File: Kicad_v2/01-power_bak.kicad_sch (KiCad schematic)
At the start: 45 parts, among them IC2 BQ25630YBGR, J1 USB4105-GF-A-060, U11 RT6158HWSC, U2 TCR3UG33A_LF, U4 TPS61253F, U7 USBLC6-2SC6

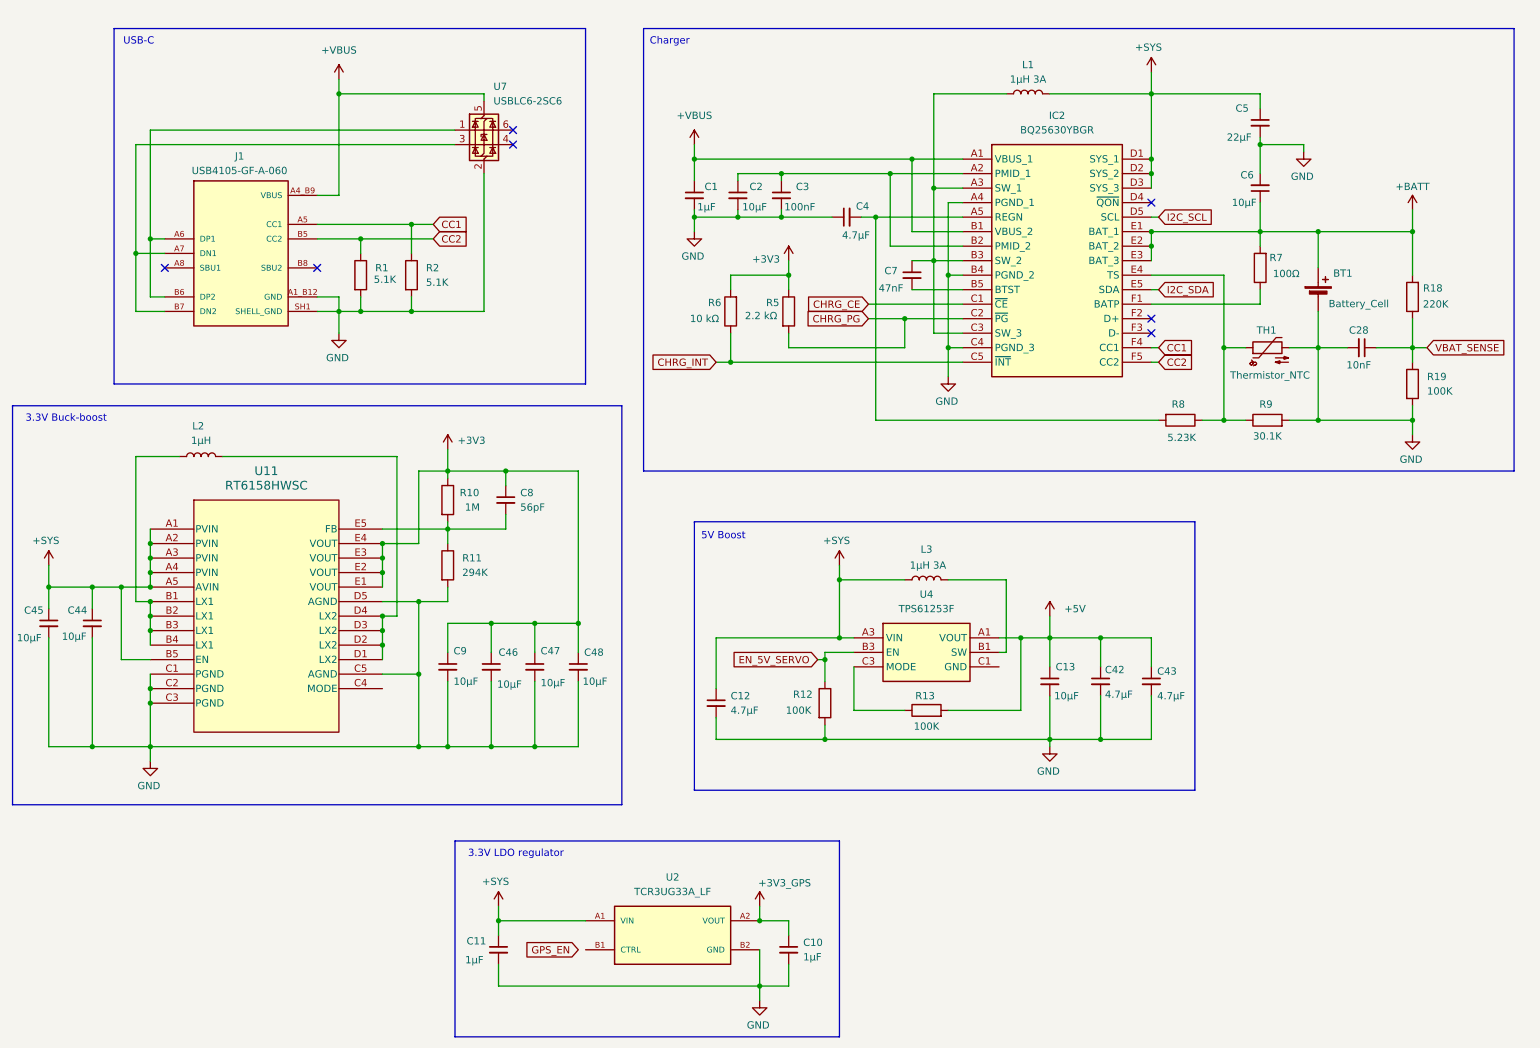
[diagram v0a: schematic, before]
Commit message: KiCad Power schema herschikt
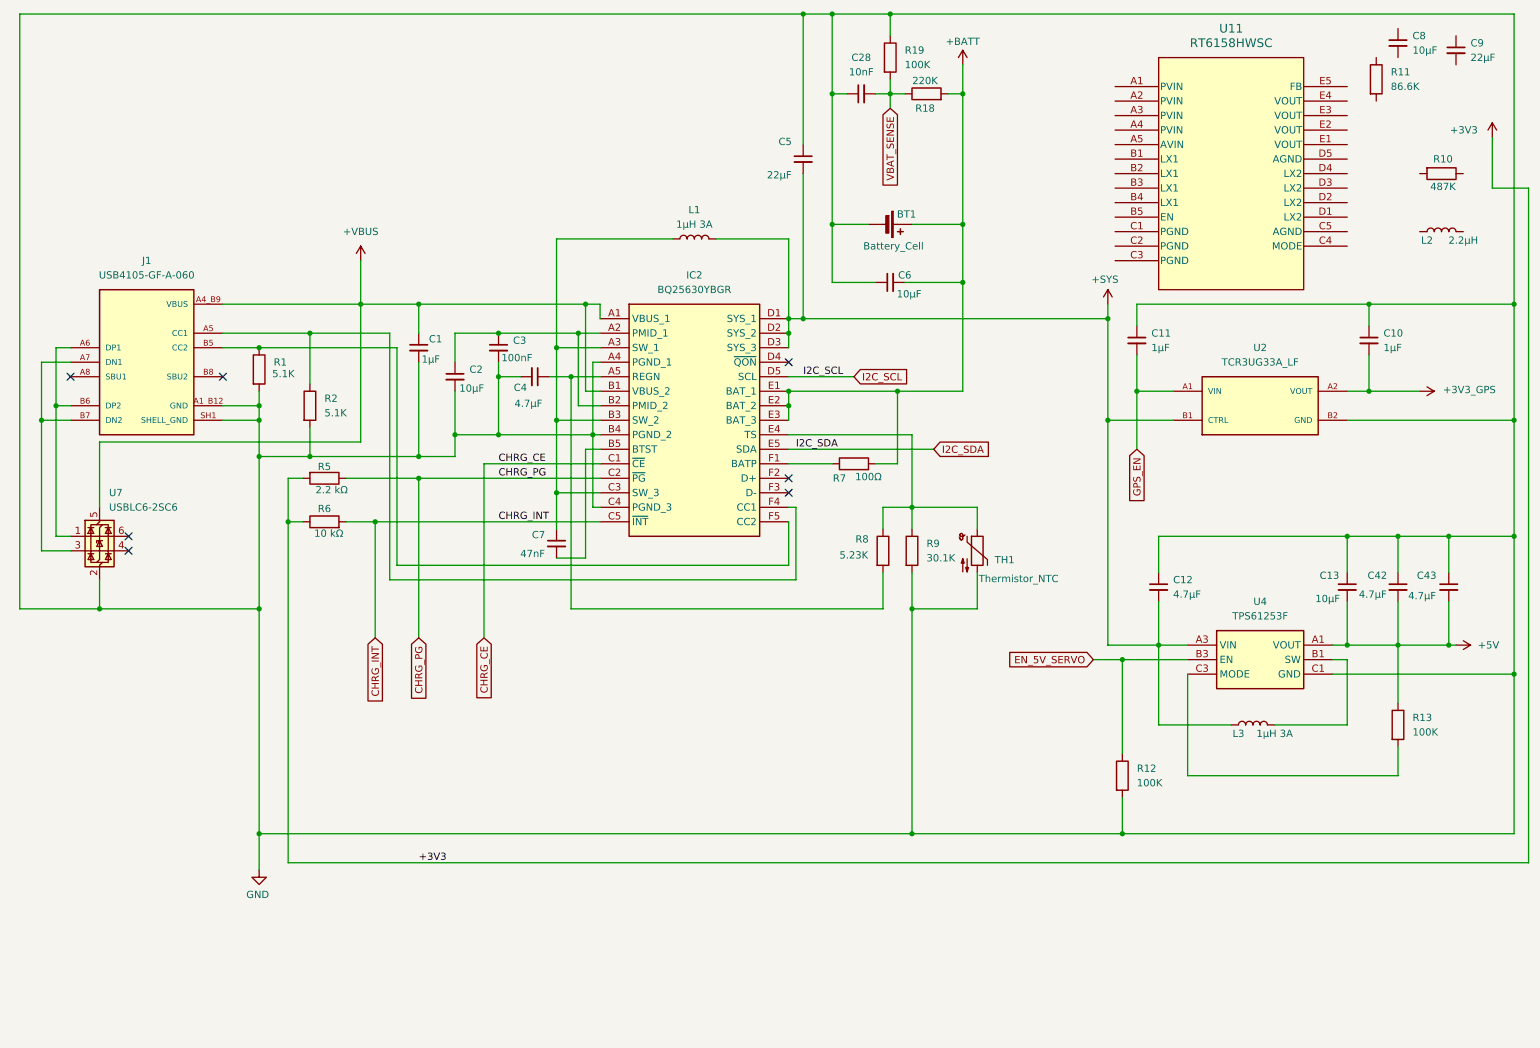
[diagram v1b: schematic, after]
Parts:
- removed C44, C45, C46, C47, C48: 10µF, Capacitor_SMD:C_0603_1608Metric_Pad1.08x0.95mm_HandSolder, symbol Device:C_Small
- C8: value 56pF -> 10µF
- C9: value 10µF -> 22µF
- L2: value 1µH -> 2.2µH
- R10: value 1M -> 487K
- R11: value 294K -> 86.6K
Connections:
- net +3V3: now also R5.2, R6.1; no longer C8.1, C9.1, R10.1, R5.1, R6.2, U11.E1 (VOUT), U11.E2 (VOUT), U11.E3 (VOUT), U11.E4 (VOUT)
- net +3V3_GPS: now also C10.2; no longer C10.1
- net +5V: now also C13.2, C42.2, C43.2, R13.1; no longer C13.1, C42.1, C43.1, R13.2
- net +BATT: now also C6.2; no longer C6.1
- net +SYS: now also C12.2, C5.2, U2.B1 (CTRL); no longer C11.1, C12.1, C5.1, U11.A1 (PVIN), U11.A2 (PVIN), U11.A3 (PVIN), U11.A4 (PVIN), U11.A5 (AVIN), U11.B5 (EN), U2.A1 (VIN)
- net CHRG_INT: now also R6.2; no longer R6.1
- net CHRG_PG: now also R5.1; no longer R5.2
- net GND: now also C10.1, C11.1, C12.1, C13.1, C28.1, C4.2, C42.1, C43.1, C5.1, C6.1, R19.1, U4.C1 (GND), U4.C2 (GND); no longer C10.2, C11.2, C12.2, C13.2, C28.2, C4.1, C42.2, C43.2, C5.2, C6.2, C9.2, R11.2, R19.2, U11.C1 (PGND), U11.C2 (PGND), U11.C3 (PGND), U11.C5 (AGND), U11.D5 (AGND)
- net GPS_EN: now also C11.2, U2.A1 (VIN)
- net VBAT_SENSE: now also C28.2, R19.2; no longer C28.1, R19.1
- net at U4.C3 (MODE): now also R13.2; no longer R13.1
- net at IC2.A5 (REGN), R8.2: now also C4.1; no longer C4.2
- net CC1: no longer names the net of IC2.F4 (CC1), J1.A5 (CC1), R2.1
- net CC2: no longer names the net of IC2.F5 (CC2), J1.B5 (CC2), R1.1
- now unconnected: C8.2, L2.1, L2.2, R10.2, R11.1, U11.B1 (LX1), U11.B2 (LX1), U11.B3 (LX1), U11.B4 (LX1), U11.D1 (LX2), U11.D2 (LX2), U11.D3 (LX2), U11.D4 (LX2), U11.E5 (FB)
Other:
- note removed: "3.3V Buck-boost"
- note removed: "3.3V LDO regulator"
- note removed: "5V Boost"
- note removed: "Charger"
- note removed: "USB-C"
- moved on the sheet: BT1, C1, C10, C11, C12, C13, C2, C28, C3, C4, C42, C43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
